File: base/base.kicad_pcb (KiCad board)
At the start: 2 copper layers, 100 x 100 mm, 25 parts, among them J1 FTDI, J2 Barrel_Jack, J3 CONN_01X40, SW1 SW_Push, U1 Z80CPU, U2 27C256, U3 7404, U4 55257, U5 7432, U6 16550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

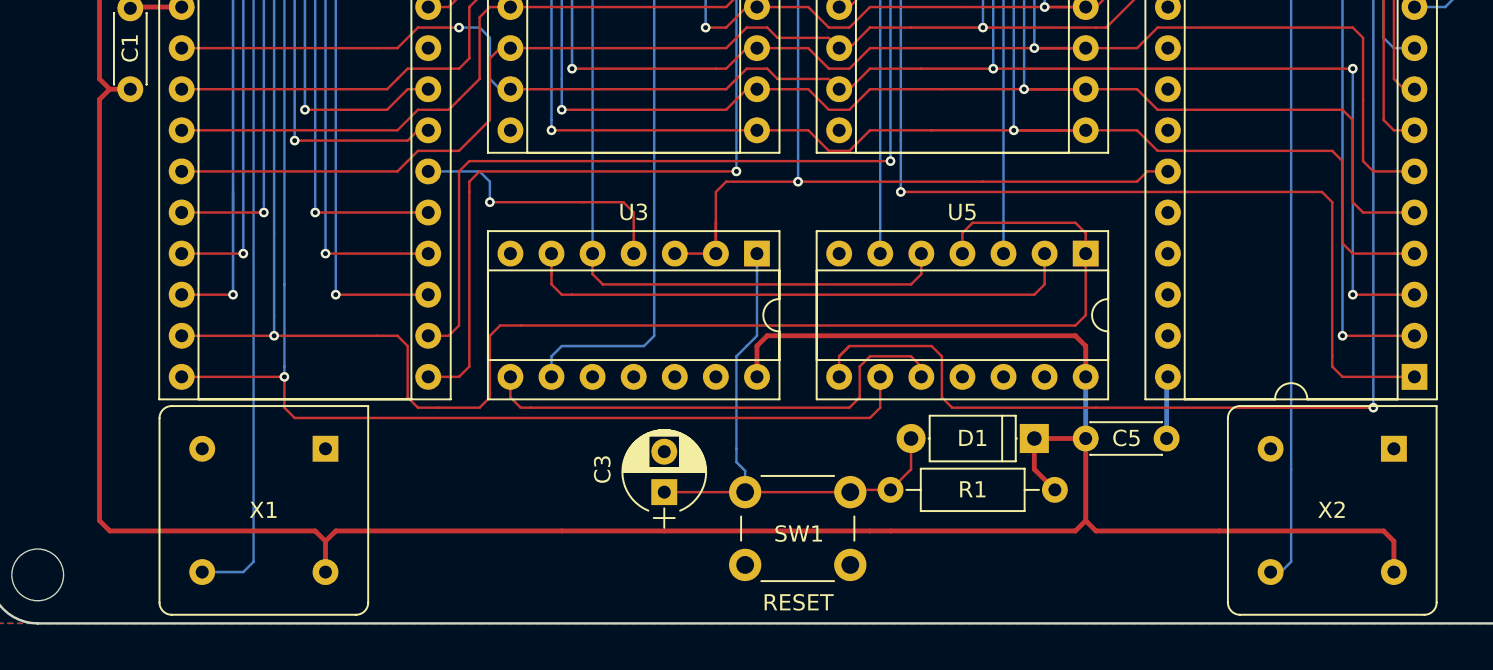
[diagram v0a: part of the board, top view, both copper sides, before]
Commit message: Change reset switch to right angle
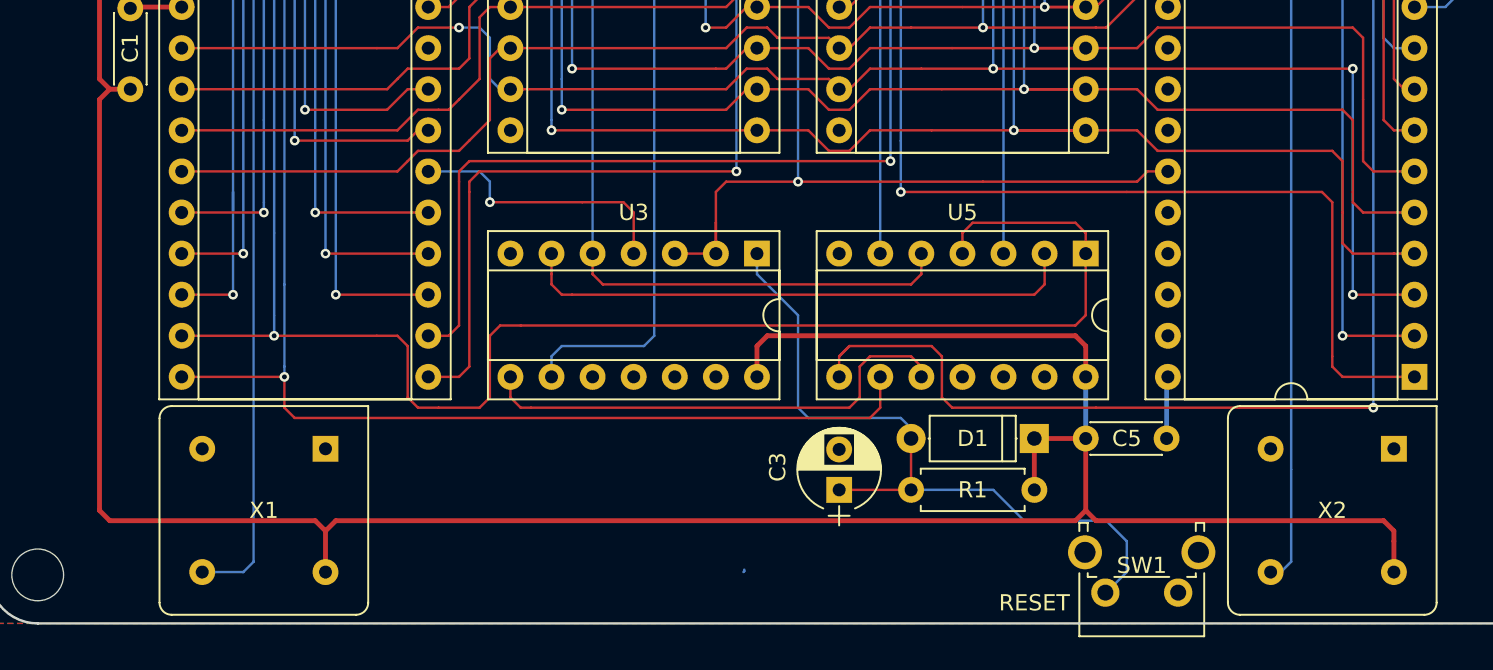
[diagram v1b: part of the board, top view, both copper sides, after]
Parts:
- R1: footprint Resistors_THT:R_Axial_DIN0207_L6.3mm_D2.5mm_P10.16mm_Horizontal -> Resistors_THT:R_Axial_DIN0207_L6.3mm_D2.5mm_P7.62mm_Horizontal
- SW1: footprint Buttons_Switches_THT:SW_PUSH_6mm_h5mm -> Buttons_Switches_THT:SW_Tactile_SPST_Angled_PTS645Vx31-2LFS
- moved SW1 20.3 mm to (127.6, 158.1)
- moved C3 10.8 mm to (106.7, 151.8)
- moved R1 1.27 mm to (118.7, 151.8)
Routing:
- net Net-(C3-Pad1): track 33.2 -> 45.4 mm
- net +5V: track 374.6 -> 373.4 mm

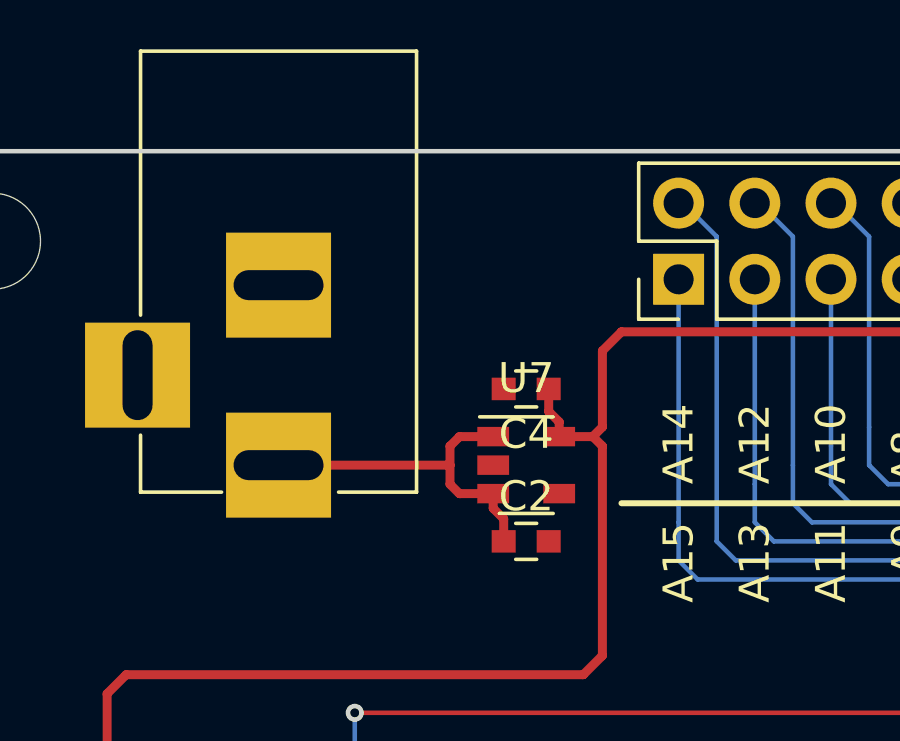
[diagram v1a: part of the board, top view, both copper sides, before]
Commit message: Moved voltage regulator
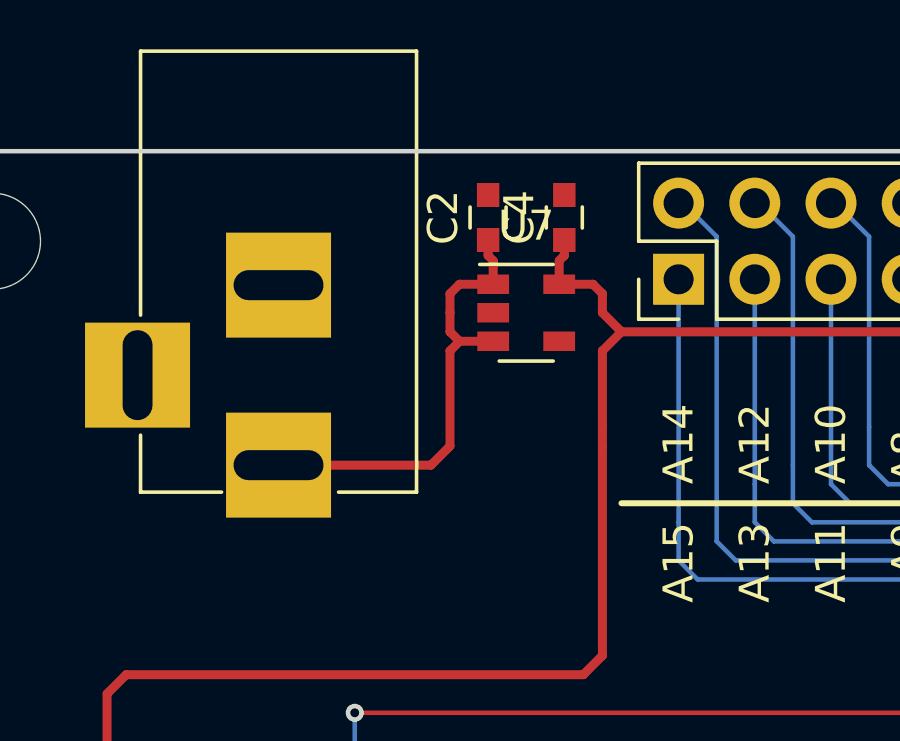
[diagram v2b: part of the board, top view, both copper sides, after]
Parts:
- moved C2 10.9 mm to (73.7, 62.2), turned to 90 degrees
- moved C4 5.85 mm to (76.2, 62.2), turned to 90 degrees
- moved U7 5.08 mm to (74.9, 65.4)
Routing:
- net Net-(C2-Pad1): track 11.9 -> 15.6 mm
- net +5V: track 373.4 -> 374.9 mm
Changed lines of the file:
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@@
     (thickness 1.6)
     (drawings 57)
-    (tracks 1094)
+    (tracks 1099)
     (zones 0)
     (modules 25)
@@
   )
   (module Capacitors_SMD:C_0603 (layer F.Cu)
-    (at 74.93 73.025)
+    (at 73.66 62.23 90)
     (descr "Capacitor SMD 0603, reflow soldering, AVX (see smccp.pdf)")
     (tags "capacitor 0603")
     (attr smd)
-    (fp_text reference C2 (at 0 -1.5) (layer F.SilkS)
-      (effects (font (size 1 1) (thickness 0.15)))
-    )
-    (fp_text value "1 uF" (at 0 1.5) (layer F.Fab)
-      (effects (font (size 1 1) (thickness 0.15)))
-    )
-    (fp_text user %R (at 0 0) (layer F.Fab)
+    (fp_text reference C2 (at 0 -1.5 90) (layer F.SilkS)
+      (effects (font (size 1 1) (thickness 0.15)))
+    )
+    (fp_text value "1 uF" (at 0 1.5 90) (layer F.Fab)
+      (effects (font (size 1 1) (thickness 0.15)))
+    )
+    (fp_text user %R (at 0 0 90) (layer F.Fab)
       (effects (font (size 0.3 0.3) (thickness 0.075)))
     )
@@
     (fp_line (start 1.4 0.65) (end 1.4 -0.65) (layer F.CrtYd) (width 0.05))
     (fp_line (start 1.4 0.65) (end -1.4 0.65) (layer F.CrtYd) (width 0.05))
-    (pad 1 smd rect (at -0.75 0) (size 0.8 0.75) (layers F.Cu F.Paste F.Mask)
+    (pad 1 smd rect (at -0.75 0 90) (size 0.8 0.75) (layers F.Cu F.Paste F.Mask)
       (net 72 "Net-(C2-Pad1)"))
-    (pad 2 smd rect (at 0.75 0) (size 0.8 0.75) (layers F.Cu F.Paste F.Mask)
+    (pad 2 smd rect (at 0.75 0 90) (size 0.8 0.75) (layers F.Cu F.Paste F.Mask)
       (net 18 GND))
     (model Capacitors_SMD.3dshapes/C_0603.wrl
@@
   )
   (module Capacitors_SMD:C_0603 (layer F.Cu)
-    (at 74.93 67.945 180)
+    (at 76.2 62.23 90)
     (descr "Capacitor SMD 0603, reflow soldering, AVX (see smccp.pdf)")
     (tags "capacitor 0603")
     (attr smd)
-    (fp_text reference C4 (at 0 -1.5 180) (layer F.SilkS)
-      (effects (font (size 1 1) (thickness 0.15)))
-    )
-    (fp_text value "1 uF" (at 0 1.5 180) (layer F.Fab)
+    (fp_text reference C4 (at 0 -1.5 90) (layer F.SilkS)
+      (effects (font (size 1 1) (thickness 0.15)))
+    )
+    (fp_text value "1 uF" (at 0 1.5 90) (layer F.Fab)
       (effects (font (size 1 1) (thickness 0.15)))
     )
@@
     (fp_line (start 0.8 0.4) (end -0.8 0.4) (layer F.Fab) (width 0.1))
     (fp_line (start -0.8 0.4) (end -0.8 -0.4) (layer F.Fab) (width 0.1))
-    (fp_text user %R (at 0 0 180) (layer F.Fab)
+    (fp_text user %R (at 0 0 90) (layer F.Fab)
       (effects (font (size 0.3 0.3) (thickness 0.075)))
     )
-    (pad 2 smd rect (at 0.75 0 180) (size 0.8 0.75) (layers F.Cu F.Paste F.Mask)
+    (pad 2 smd rect (at 0.75 0 90) (size 0.8 0.75) (layers F.Cu F.Paste F.Mask)
       (net 18 GND))
-    (pad 1 smd rect (at -0.75 0 180) (size 0.8 0.75) (layers F.Cu F.Paste F.Mask)
+    (pad 1 smd rect (at -0.75 0 90) (size 0.8 0.75) (layers F.Cu F.Paste F.Mask)
       (net 15 +5V))
     (model Capacitors_SMD.3dshapes/C_0603.wrl
@@
   )
   (module TO_SOT_Packages_SMD:SOT-23-5 (layer F.Cu)
-    (at 74.93 70.485)
+    (at 74.93 65.405)
     (descr "5-pin SOT23 package")
     (tags SOT-23-5)
@@
   (segment (start 100.965 115.57) (end 102.235 115.57) (width 0.152) (layer F.Cu) (net 14))
   (segment (start 99.695 116.84) (end 100.965 115.57) (width 0.152) (layer F.Cu) (net 14))
+  (segment (start 78.105 66.04) (end 77.47 65.405) (width 0.3) (layer F.Cu) (net 15))
+  (segment (start 77.155 64.455) (end 76.03 64.455) (width 0.3) (layer F.Cu) (net 15) (status 800000))
+  (segment (start 77.47 64.77) (end 77.155 64.455) (width 0.3) (layer F.Cu) (net 15))
+  (segment (start 77.47 65.405) (end 77.47 64.77) (width 0.3) (layer F.Cu) (net 15))
+  (segment (start 77.47 69.215) (end 77.47 69.85) (width 0.3) (layer F.Cu) (net 15))
+  (segment (start 76.03 64.455) (end 76.03 63.67) (width 0.3) (layer F.Cu) (net 15) (status 400000))
+  (segment (start 76.03 63.67) (end 76.2 63.5) (width 0.3) (layer F.Cu) (net 15))
+  (segment (start 76.2 63.5) (end 76.2 62.98) (width 0.3) (layer F.Cu) (net 15) (status 800000))
   (segment (start 74.93 154.305) (end 74.93 156.845) (width 0.3) (layer F.Cu) (net 15) (status 800000))
   (segment (start 121.92 153.035) (end 122.555 153.67) (width 0.3) (layer F.Cu) (net 15))
@@
   (segment (start 61.595 153.67) (end 74.295 153.67) (width 0.3) (layer F.Cu) (net 15))
   (segment (start 118.745 148.59) (end 118.745 151.765) (width 0.3) (layer F.Cu) (net 15) (status C00000))
-  (segment (start 77.15 69.535) (end 77.155 69.535) (width 0.3) (layer F.Cu) (net 15))
   (segment (start 60.96 93.345) (end 61.595 93.98) (width 0.3) (layer F.Cu) (net 15))
+  (segment (start 77.47 69.85) (end 77.47 76.835) (width 0.3) (layer F.Cu) (net 15))
+  (segment (start 77.47 76.835) (end 76.835 77.47) (width 0.3) (layer F.Cu) (net 15))
+  (segment (start 76.835 77.47) (end 61.595 77.47) (width 0.3) (layer F.Cu) (net 15))
+  (segment (start 61.595 77.47) (end 60.96 78.105) (width 0.3) (layer F.Cu) (net 15))
   (segment (start 60.96 78.105) (end 60.96 93.345) (width 0.3) (layer F.Cu) (net 15))
-  (segment (start 61.595 77.47) (end 60.96 78.105) (width 0.3) (layer F.Cu) (net 15))
-  (segment (start 76.835 77.47) (end 61.595 77.47) (width 0.3) (layer F.Cu) (net 15))
-  (segment (start 77.47 76.835) (end 76.835 77.47) (width 0.3) (layer F.Cu) (net 15))
-  (segment (start 77.47 69.85) (end 77.47 76.835) (width 0.3) (layer F.Cu) (net 15))
-  (segment (start 77.155 69.535) (end 77.47 69.85) (width 0.3) (layer F.Cu) (net 15))
-  (segment (start 76.03 69.535) (end 77.15 69.535) (width 0.3) (layer F.Cu) (net 15) (status 400000))
   (segment (start 100.33 65.405) (end 100.33 64.29) (width 0.3) (layer F.Cu) (net 15) (status 800000))
   (segment (start 99.695 66.04) (end 100.33 65.405) (width 0.3) (layer F.Cu) (net 15))
@@
   (segment (start 77.47 66.675) (end 78.105 66.04) (width 0.3) (layer F.Cu) (net 15))
   (segment (start 77.47 69.215) (end 77.47 66.675) (width 0.3) (layer F.Cu) (net 15))
-  (segment (start 77.15 69.535) (end 77.47 69.215) (width 0.3) (layer F.Cu) (net 15))
-  (segment (start 76.03 69.535) (end 76.03 69.045) (width 0.3) (layer F.Cu) (net 15) (status 400000))
-  (segment (start 75.68 68.695) (end 75.68 67.945) (width 0.3) (layer F.Cu) (net 15) (status 800000))
-  (segment (start 76.03 69.045) (end 75.68 68.695) (width 0.3) (layer F.Cu) (net 15))
   (segment (start 61.595 93.98) (end 100.965 93.98) (width 0.3) (layer F.Cu) (net 15))
   (segment (start 100.965 93.98) (end 101.6 94.615) (width 0.3) (layer F.Cu) (net 15))
@@
   (segment (start 127 80.01) (end 127 62.865) (width 0.152) (layer B.Cu) (net 70))
   (segment (start 125.885 61.75) (end 125.73 61.75) (width 0.152) (layer B.Cu) (net 70) (status C00000))
-  (segment (start 72.39 70.485) (end 66.675 70.485) (width 0.3) (layer F.Cu) (net 72) (status 800000))
-  (segment (start 73.83 71.435) (end 72.705 71.435) (width 0.3) (layer F.Cu) (net 72) (status 400000))
-  (segment (start 72.705 69.535) (end 72.39 69.85) (width 0.3) (layer F.Cu) (net 72))
-  (segment (start 72.39 69.85) (end 72.39 70.485) (width 0.3) (layer F.Cu) (net 72))
-  (segment (start 72.39 70.485) (end 72.39 71.12) (width 0.3) (layer F.Cu) (net 72))
-  (segment (start 72.705 69.535) (end 73.83 69.535) (width 0.3) (layer F.Cu) (net 72) (status 800000))
-  (segment (start 72.705 71.435) (end 72.39 71.12) (width 0.3) (layer F.Cu) (net 72))
-  (segment (start 73.83 71.435) (end 73.83 71.925) (width 0.3) (layer F.Cu) (net 72) (status 400000))
-  (segment (start 74.18 72.275) (end 74.18 73.025) (width 0.3) (layer F.Cu) (net 72) (status 800000))
-  (segment (start 73.83 71.925) (end 74.18 72.275) (width 0.3) (layer F.Cu) (net 72))
+  (segment (start 72.705 66.355) (end 72.705 66.36) (width 0.3) (layer F.Cu) (net 72))
+  (segment (start 71.755 70.485) (end 66.675 70.485) (width 0.3) (layer F.Cu) (net 72) (status 800000))
+  (segment (start 72.39 69.85) (end 71.755 70.485) (width 0.3) (layer F.Cu) (net 72))
+  (segment (start 72.39 66.675) (end 72.39 69.85) (width 0.3) (layer F.Cu) (net 72))
+  (segment (start 72.705 66.36) (end 72.39 66.675) (width 0.3) (layer F.Cu) (net 72))
+  (segment (start 73.83 66.355) (end 72.705 66.355) (width 0.3) (layer F.Cu) (net 72) (status 400000))
+  (segment (start 72.705 64.455) (end 72.39 64.77) (width 0.3) (layer F.Cu) (net 72))
+  (segment (start 72.39 64.77) (end 72.39 65.405) (width 0.3) (layer F.Cu) (net 72))
+  (segment (start 72.705 64.455) (end 73.83 64.455) (width 0.3) (layer F.Cu) (net 72) (status 800000))
+  (segment (start 72.39 66.04) (end 72.39 65.405) (width 0.3) (layer F.Cu) (net 72))
+  (segment (start 72.705 66.355) (end 72.39 66.04) (width 0.3) (layer F.Cu) (net 72))
+  (segment (start 73.83 64.455) (end 73.83 63.67) (width 0.3) (layer F.Cu) (net 72) (status 400000))
+  (segment (start 73.66 63.5) (end 73.66 62.98) (width 0.3) (layer F.Cu) (net 72) (status 800000))
+  (segment (start 73.83 63.67) (end 73.66 63.5) (width 0.3) (layer F.Cu) (net 72))
   (zone (net 18) (net_name GND) (layer F.Cu) (hatch edge 0.508)
     (connect_pads (clearance 0.254))

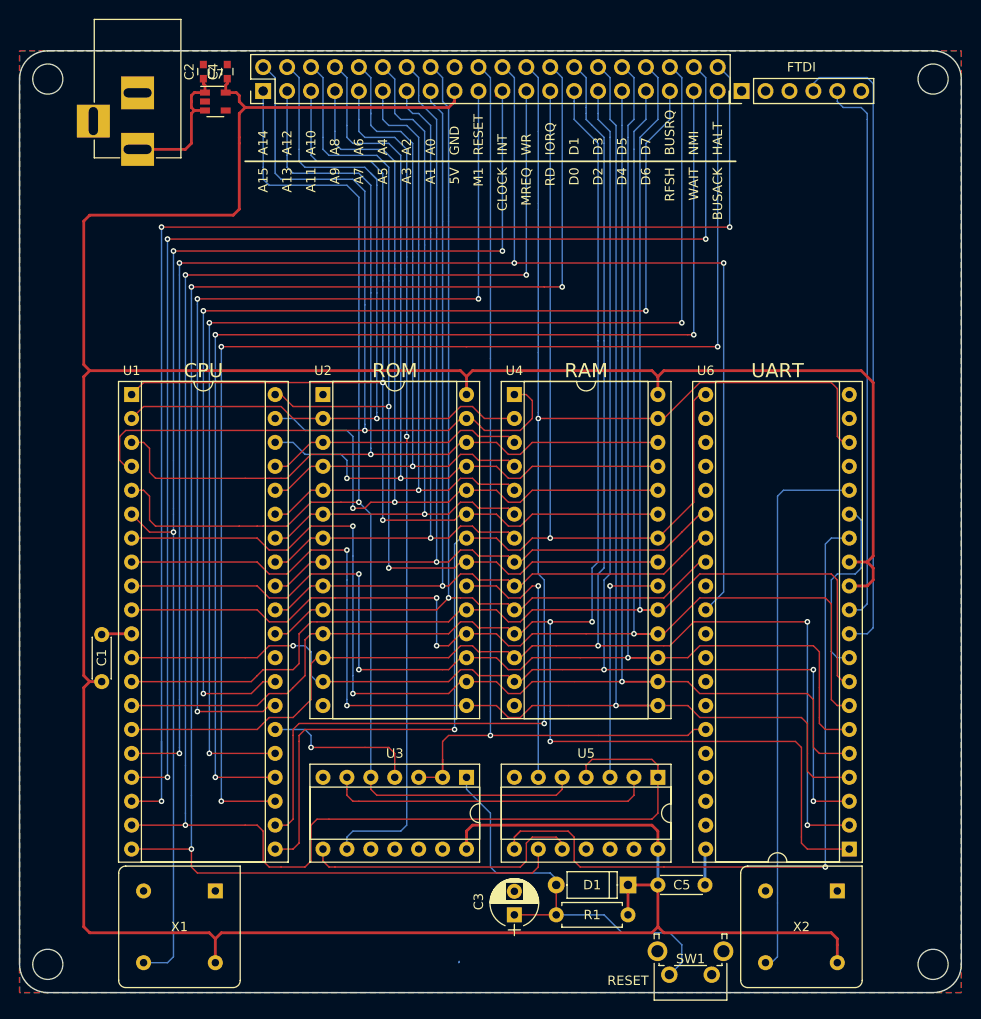
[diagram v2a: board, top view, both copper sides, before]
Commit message: Fixed capacitor sizes
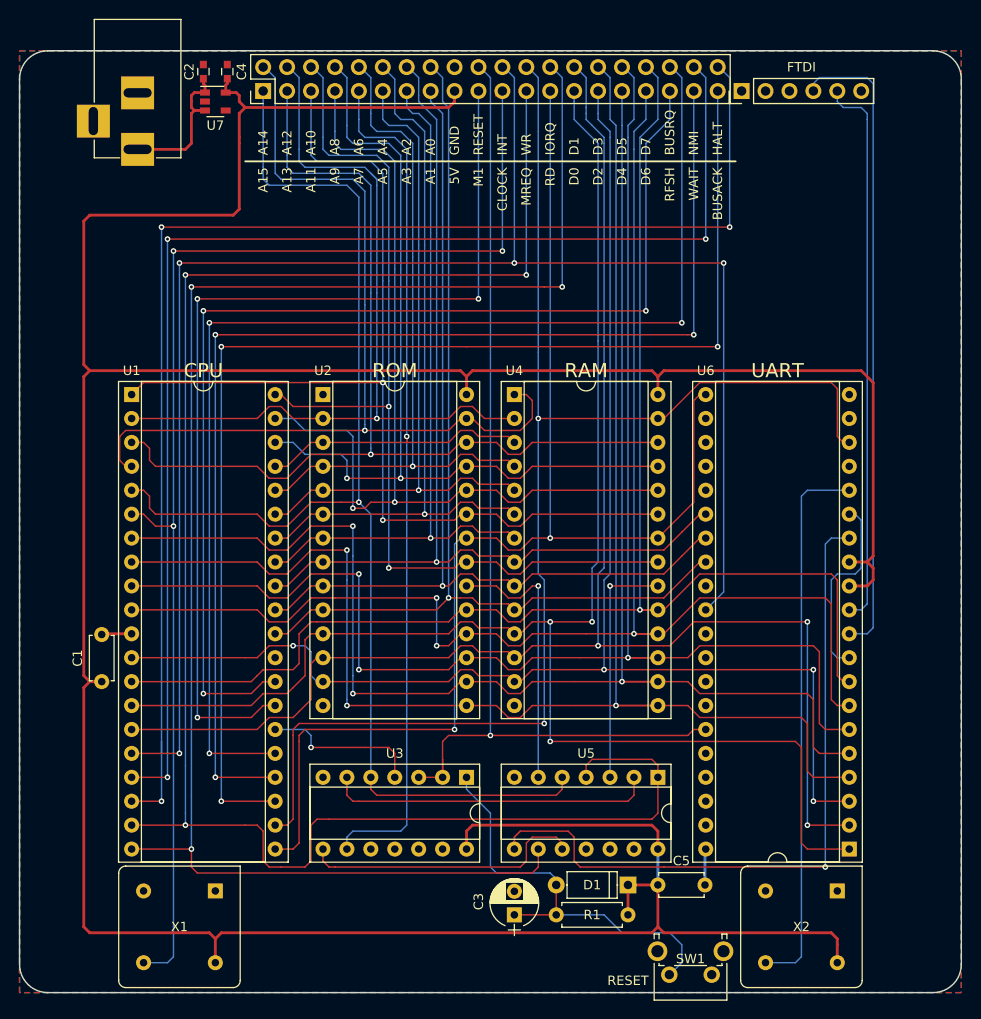
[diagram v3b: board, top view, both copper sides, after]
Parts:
- removed REF** (x4): MountingHole_3.2mm_M3, Mounting_Holes:MountingHole_3.2mm_M3
- removed REF***: OSHW-Symbol_6.7x6mm_SilkScreen, Symbols:OSHW-Symbol_6.7x6mm_SilkScreen
- C1: value 1 uF -> .1 uF; footprint Capacitors_THT:C_Disc_D4.3mm_W1.9mm_P5.00mm -> Capacitors_THT:C_Disc_D4.7mm_W2.5mm_P5.00mm
- C5: value C_Small -> .1 uF; footprint Capacitors_THT:C_Disc_D4.3mm_W1.9mm_P5.00mm -> Capacitors_THT:C_Disc_D4.7mm_W2.5mm_P5.00mm
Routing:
- net M1: track 104.2 -> 105.8 mm
- net /A15: track 135.3 -> 134.6 mm
- net /A13: track 107.9 -> 107.2 mm
- net Net-(U6-Pad16): track 58.3 -> 58.9 mm
